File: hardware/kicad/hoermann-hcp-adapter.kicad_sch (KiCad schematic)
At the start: 5 parts, among them J1 HCP2 6P6C unshielded, AliExpr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, U1 ESP32-C3 Super Mini, U2 Isolated auto-direction RS485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

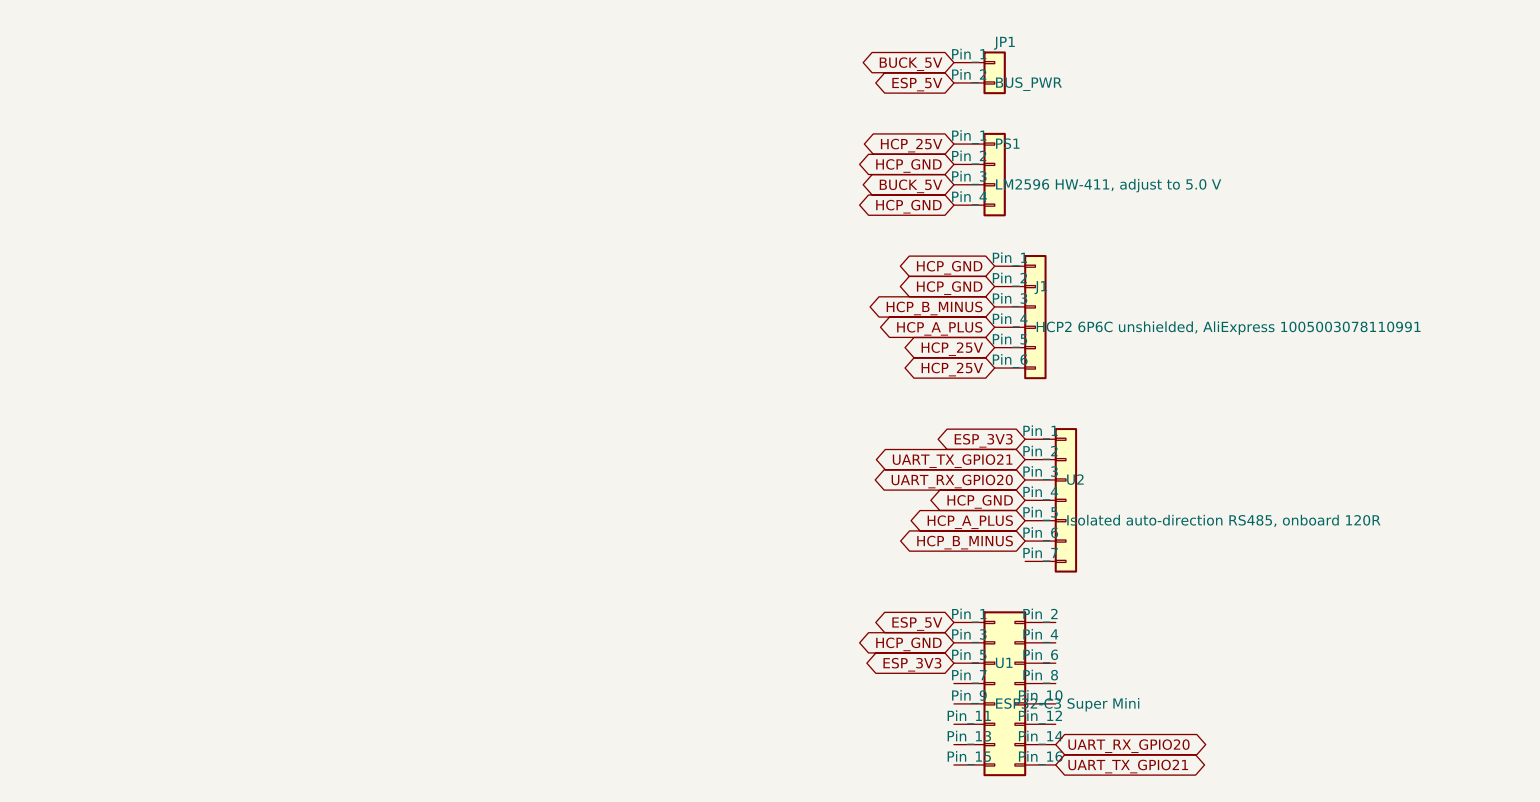
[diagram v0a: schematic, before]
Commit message: Draw visible schematic connections
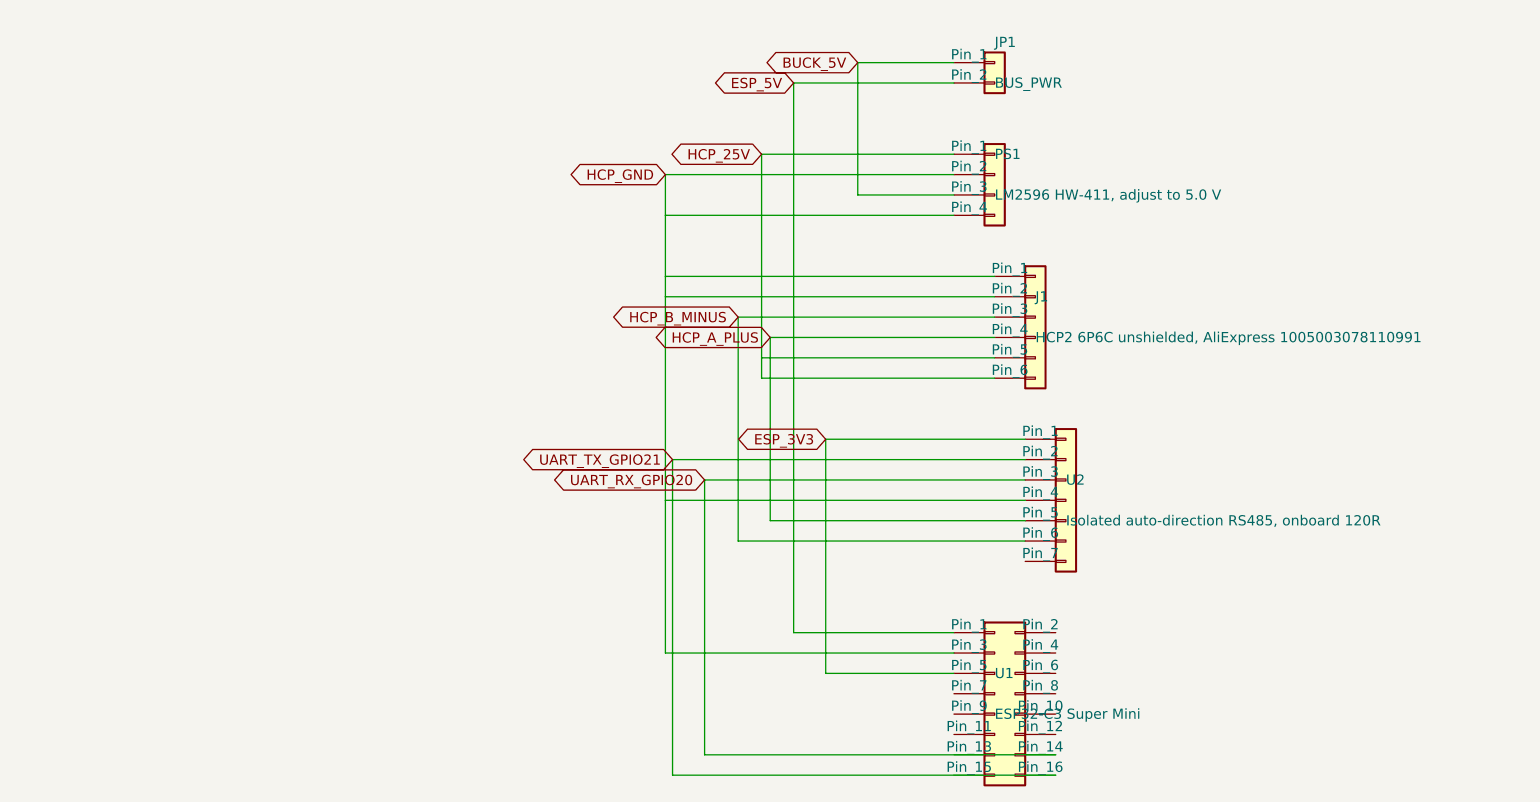
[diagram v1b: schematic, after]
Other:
- moved on the sheet: J1, PS1, U1

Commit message: Arrange schematic around ESP32
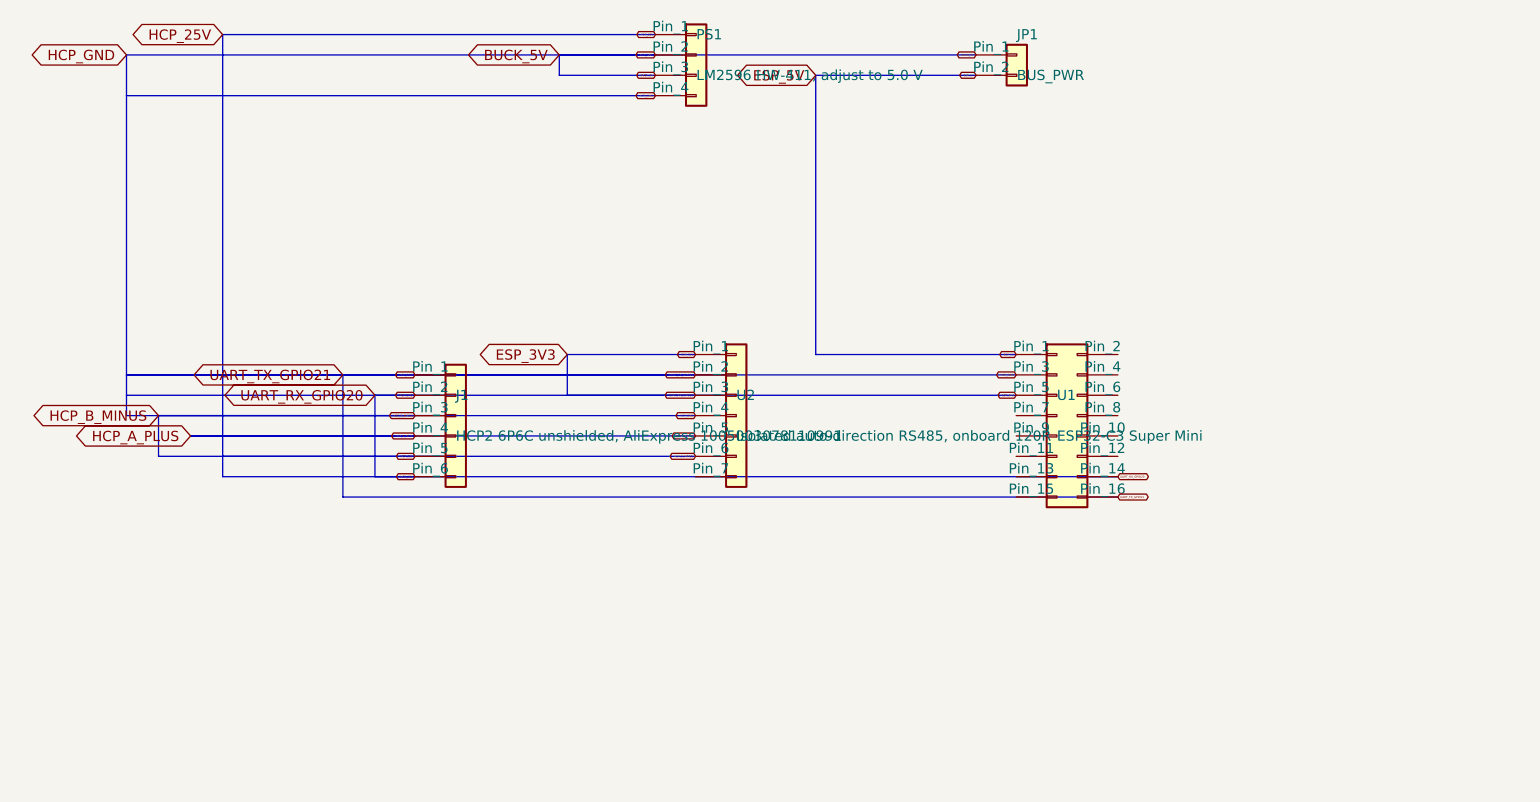
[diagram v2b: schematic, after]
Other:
- moved on the sheet: J1, JP1, PS1, U1, U2
